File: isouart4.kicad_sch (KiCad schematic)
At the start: 14 parts, among them J1 USB_B, J2 Conn_01x04, J3 Conn_01x04, J4 Conn_01x04, J5 Conn_01x04, U3 AMS1117-3.3, U6 π122U31, U7 π122U31, U8 π122U31, U9 π122U31

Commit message: Flush
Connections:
- net indicators-ch2/GNDMON: now reaches J3.1 (Pin_1), U7.5 (GND2)
- net indicators-ch2/TXMON: now reaches J3.2 (Pin_2), U7.6 (VOB)
- net indicators-ch2/RXMON: now reaches J3.3 (Pin_3), U7.7 (VOA)
- net indicators-ch2/V+MON: now reaches J3.4 (Pin_4), U7.8 (VDD2)
- net indicators-ch1/TXMON: now reaches J2.2 (Pin_2), U6.6 (VOB)
- net indicators-ch1/RXMON: now reaches J2.3 (Pin_3), U6.7 (VIA)
- net indicators-ch1/V+MON: now reaches J2.4 (Pin_4), U6.8 (VDD2)
- net indicators-ch4/GNDMON: now reaches J5.1 (Pin_1), U9.5 (GND2)
- net indicators-ch4/TXMON: now reaches J5.2 (Pin_2), U9.6 (VOB)
- net indicators-ch4/RXMON: now reaches J5.3 (Pin_3), U9.7 (VOA)
- net indicators-ch4/V+MON: now reaches J5.4 (Pin_4), U9.8 (VDD2)
- net indicators-ch3/GNDMON: now reaches J4.1 (Pin_1), U8.5 (GND2)
- net indicators-ch3/TXMON: now reaches J4.2 (Pin_2), U8.6 (VOB)
- net indicators-ch3/RXMON: now reaches J4.3 (Pin_3), U8.7 (VOA)
- net indicators-ch3/V+MON: now reaches J4.4 (Pin_4), U8.8 (VDD2)
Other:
- sheet indicators-ch1 ports: added GNDMON, RXMON, TXMON, V+MON; removed none
- sheet indicators-ch2 ports: added GNDMON, RXMON, TXMON, V+MON; removed none
- sheet indicators-ch3 ports: added GNDMON, RXMON, TXMON, V+MON; removed none
- sheet indicators-ch4 ports: added GNDMON, RXMON, TXMON, V+MON; removed none

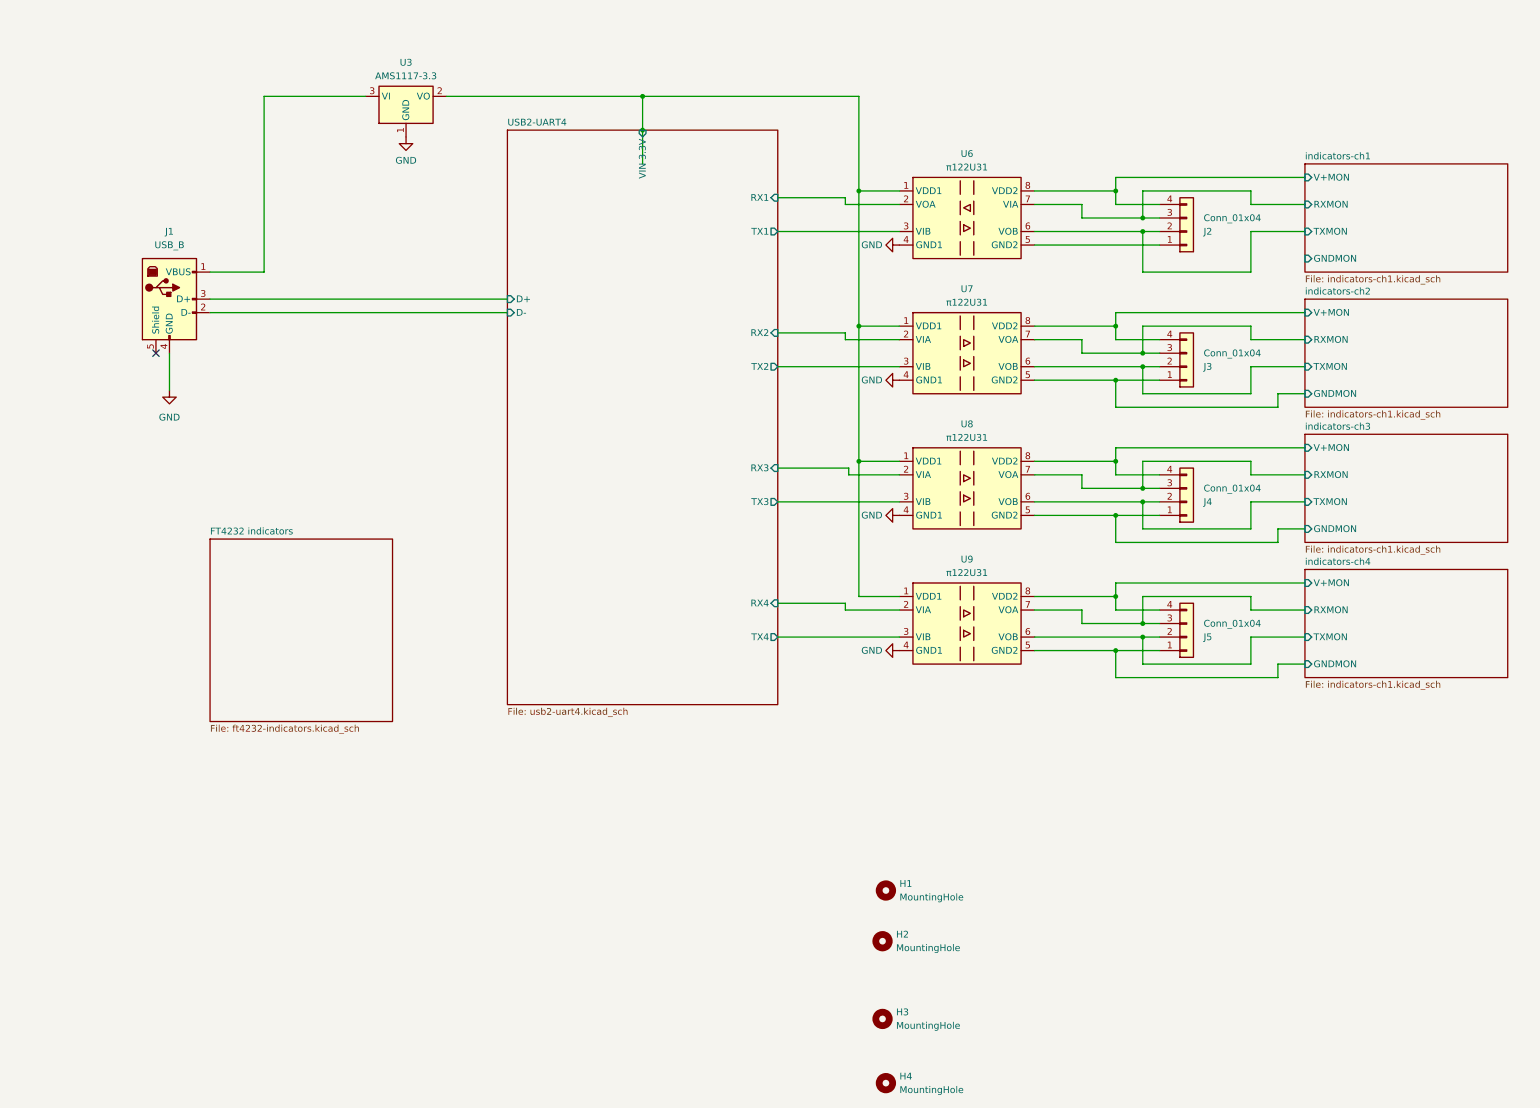
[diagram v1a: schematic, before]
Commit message: switch to CH344Q
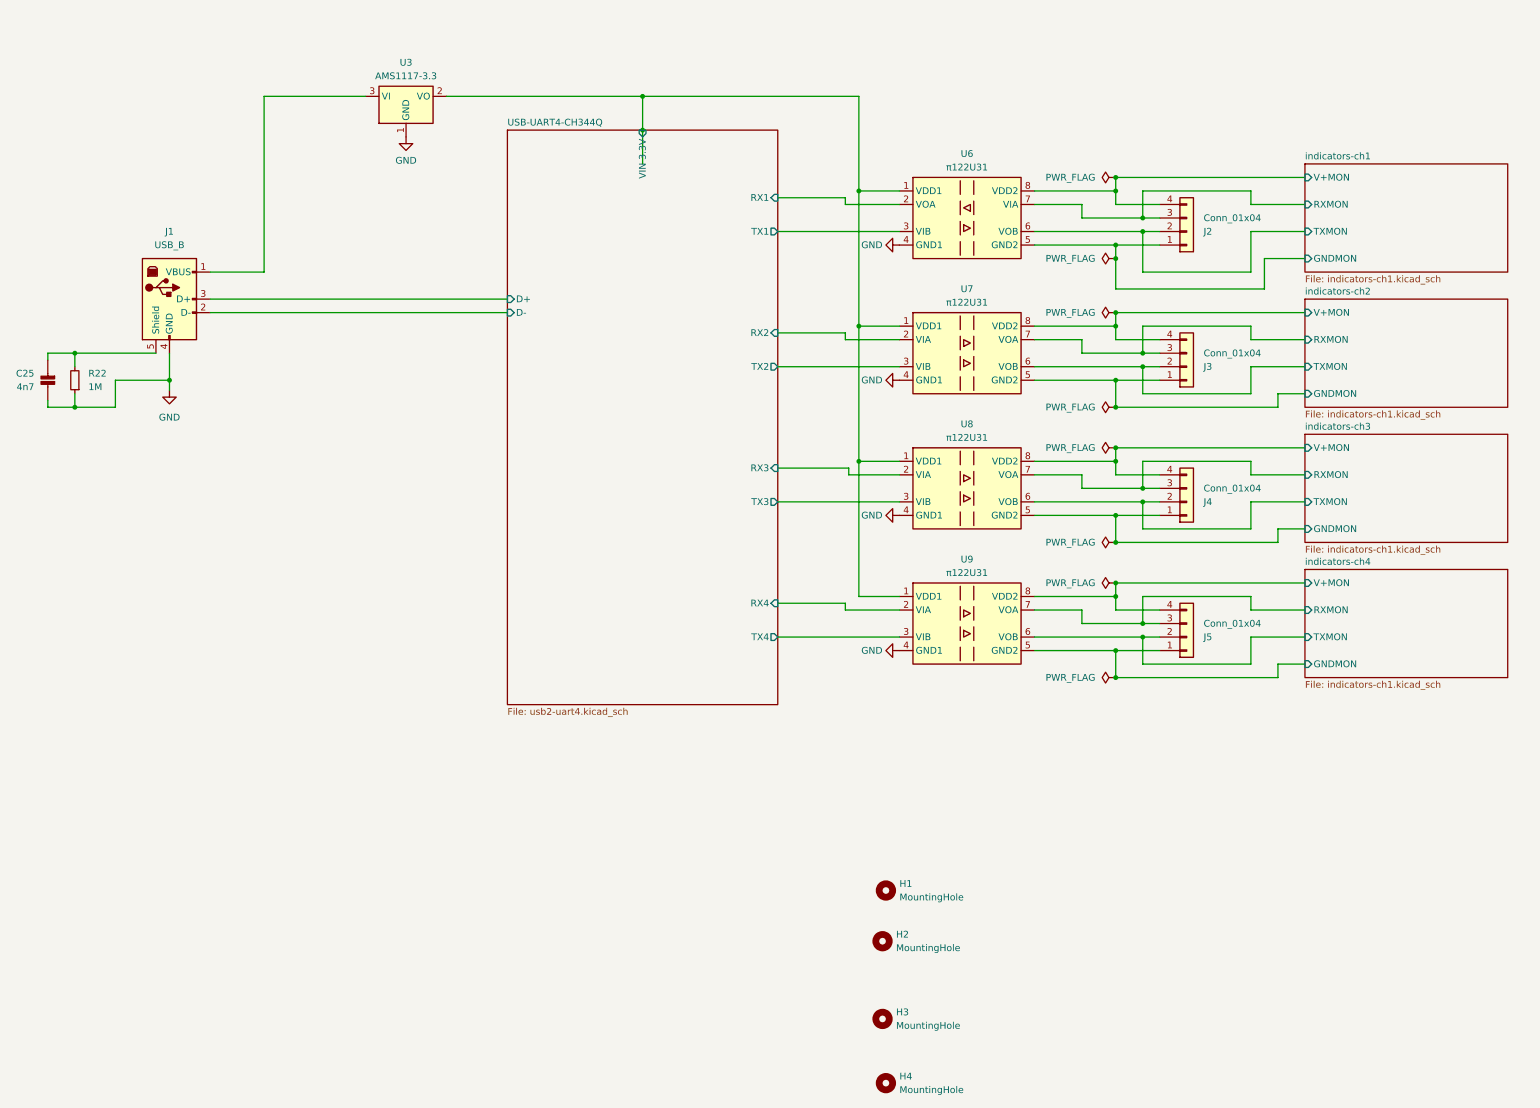
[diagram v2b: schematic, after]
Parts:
- added C25: 4n7, Capacitor_SMD:C_0805_2012Metric_Pad1.18x1.45mm_HandSolder, symbol H_passives:CAP_NP
- added R22: 1M, Resistor_SMD:R_0805_2012Metric_Pad1.20x1.40mm_HandSolder, symbol Device:R_Small
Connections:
- net GND: now also C25.1, R22.1
- net indicators-ch1/GNDMON: now also J2.1 (Pin_1), U6.5 (GND2)
- net at J1.5 (Shield): now also C25.2, R22.2
- no-connect marks 1 -> 0
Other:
- sheet USB2-UART4 renamed USB-UART4-CH344Q
- removed sheet FT4232 indicators

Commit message: More feng shui
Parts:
- removed C25: 4n7, Capacitor_SMD:C_0805_2012Metric_Pad1.18x1.45mm_HandSolder, symbol H_passives:CAP_NP
- removed R22: 1M, Resistor_SMD:R_0805_2012Metric_Pad1.20x1.40mm_HandSolder, symbol Device:R_Small
- removed U7, U8, U9: π122U31, Package_SO:SOIC-8_3.9x4.9mm_P1.27mm, symbol Isolator:π120U31
- added C2, C7: 10uF, Capacitor_SMD:C_0805_2012Metric_Pad1.18x1.45mm_HandSolder, symbol Device:C_Polarized_Small
- added C44: 100n, Capacitor_SMD:C_0603_1608Metric_Pad1.08x0.95mm_HandSolder, symbol H_passives:CAP_NP
- added L1, L2: L_Ferrite_Small, Inductor_SMD:L_TDK_NLV25_2.5x2.0mm, symbol Device:L_Ferrite_Small
- added U2, U4, U5: π122U31, Package_SO:SOIC-8_3.9x4.9mm_P1.27mm, symbol Isolator:π120U31
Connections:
- net GND: now also C2.2, C44.1, C7.2, L2.2, U2.4 (GND1), U4.4 (GND1), U5.4 (GND1); no longer J1.4 (GND)
- net USB-UART4-CH344Q/RX2: now also U2.2 (VIA)
- net USB-UART4-CH344Q/RX3: now also U4.2 (VIA)
- net USB-UART4-CH344Q/RX4: now also U5.2 (VIA)
- net USB-UART4-CH344Q/TX2: now also U2.3 (VIB)
- net USB-UART4-CH344Q/TX3: now also U4.3 (VIB)
- net USB-UART4-CH344Q/TX4: now also U5.3 (VIB)
- net USB-UART4-CH344Q/VIN 3.3V: now also C44.2, C7.1, U2.1 (VDD1), U4.1 (VDD1), U5.1 (VDD1)
- net indicators-ch2/GNDMON: now also U2.5 (GND2)
- net indicators-ch2/RXMON: now also U2.7 (VOA)
- net indicators-ch2/TXMON: now also U2.6 (VOB)
- net indicators-ch2/V+MON: now also U2.8 (VDD2)
- net indicators-ch3/GNDMON: now also U4.5 (GND2)
- net indicators-ch3/RXMON: now also U4.7 (VOA)
- net indicators-ch3/TXMON: now also U4.6 (VOB)
- net indicators-ch3/V+MON: now also U4.8 (VDD2)
- net indicators-ch4/GNDMON: now also U5.5 (GND2)
- net indicators-ch4/RXMON: now also U5.7 (VOA)
- net indicators-ch4/TXMON: now also U5.6 (VOB)
- net indicators-ch4/V+MON: now also U5.8 (VDD2)
- net at J1.1 (VBUS): now also L1.1; no longer U3.3 (VI)
- net USBSHLD: now reaches J1.5 (Shield)
- new net: C2.1, L1.2, U3.3 (VI)
- new net GNDUSBCONN: J1.4 (GND), L2.1
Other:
- sheet USB-UART4-CH344Q ports: added GNDUSBUART, SHLDUSB; removed none
- moved on the sheet: H1, H2, H3, H4

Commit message: pcb-route all uart channels
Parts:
- added C44 (x3): 100n, Capacitor_SMD:C_0805_2012Metric_Pad1.18x1.45mm_HandSolder, symbol H_passives:CAP_NP
- C44: footprint Capacitor_SMD:C_0603_1608Metric_Pad1.08x0.95mm_HandSolder -> Capacitor_SMD:C_0805_2012Metric_Pad1.18x1.45mm_HandSolder
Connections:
- net GND: now also C44.1, C44.1, C44.1
- net USB-UART4-CH344Q/VIN 3.3V: now also C44.2, C44.2, C44.2

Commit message: Flush latest changes
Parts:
- added C25: 4n7, Capacitor_SMD:C_0805_2012Metric_Pad1.18x1.45mm_HandSolder, symbol H_passives:CAP_NP
- added F1: 500mA, anotherfuse:FuseX, symbol Device:Fuse_Small
- added R22: 4K7, Resistor_SMD:R_0805_2012Metric_Pad1.20x1.40mm_HandSolder, symbol Device:R_Small
- H1, H2, H3, H4: footprint MountingHole:MountingHole_3.2mm_M3 -> MountingHole:MountingHole_3.2mm_M3_Pad_Via; symbol Mechanical:MountingHole -> Mechanical:MountingHole_Pad; now left out of the parts list
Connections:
- net USBSHLD: now also C25.2, R22.2
- net at J1.1 (VBUS): now also F1.1; no longer L1.1
- new net: F1.2, L1.1
- new net SHLD: C25.1, H1.1, H2.1, H3.1, H4.1, R22.1

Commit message: Add π122U31 to the project lib
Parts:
- U2, U4, U5, U6: symbol Isolator:π120U31 -> isouart4:π122U31
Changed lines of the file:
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@@
     )
   )
-  (symbol (lib_id "Isolator:π120U31") (at 213.36 137.16 0) (unit 1)
-    (in_bom yes) (on_board yes) (dnp no) (fields_autoplaced)
-    (property "Reference" "U2" (at 213.36 125.095 0)
-      (effects (font (size 1.27 1.27)))
-    )
-    (property "Value" "π122U31" (at 213.36 127.635 0)
+  (symbol (lib_id "isouart4:π122U31") (at 213.36 137.16 0) (unit 1)
+    (in_bom yes) (on_board yes) (dnp no) (fields_autoplaced)
+    (property "Reference" "U2" (at 213.36 124.46 0)
+      (effects (font (size 1.27 1.27)))
+    )
+    (property "Value" "π122U31" (at 213.36 127 0)
       (effects (font (size 1.27 1.27)))
     )
@@
     )
   )
-  (symbol (lib_id "Isolator:π120U31") (at 213.36 111.76 0) (unit 1)
-    (in_bom yes) (on_board yes) (dnp no) (fields_autoplaced)
-    (property "Reference" "U6" (at 213.36 99.695 0)
-      (effects (font (size 1.27 1.27)))
-    )
-    (property "Value" "π122U31" (at 213.36 102.235 0)
+  (symbol (lib_id "isouart4:π122U31") (at 213.36 111.76 0) (unit 1)
+    (in_bom yes) (on_board yes) (dnp no) (fields_autoplaced)
+    (property "Reference" "U6" (at 213.36 99.06 0)
+      (effects (font (size 1.27 1.27)))
+    )
+    (property "Value" "π122U31" (at 213.36 101.6 0)
       (effects (font (size 1.27 1.27)))
     )
@@
     )
   )
-  (symbol (lib_id "Isolator:π120U31") (at 213.36 187.96 0) (unit 1)
-    (in_bom yes) (on_board yes) (dnp no) (fields_autoplaced)
-    (property "Reference" "U5" (at 213.36 175.895 0)
-      (effects (font (size 1.27 1.27)))
-    )
-    (property "Value" "π122U31" (at 213.36 178.435 0)
+  (symbol (lib_id "isouart4:π122U31") (at 213.36 187.96 0) (unit 1)
+    (in_bom yes) (on_board yes) (dnp no) (fields_autoplaced)
+    (property "Reference" "U5" (at 213.36 175.26 0)
+      (effects (font (size 1.27 1.27)))
+    )
+    (property "Value" "π122U31" (at 213.36 177.8 0)
       (effects (font (size 1.27 1.27)))
     )
@@
     )
   )
-  (symbol (lib_id "Isolator:π120U31") (at 213.36 162.56 0) (unit 1)
-    (in_bom yes) (on_board yes) (dnp no) (fields_autoplaced)
-    (property "Reference" "U4" (at 213.36 150.495 0)
-      (effects (font (size 1.27 1.27)))
-    )
-    (property "Value" "π122U31" (at 213.36 153.035 0)
-      (effects (font (size 1.27 1.27)))
-    )
+  (symbol (lib_id "isouart4:π122U31") (at 213.36 162.56 0) (unit 1)
+    (in_bom yes) (on_board yes) (dnp no) (fields_autoplaced)
+    (property "Reference" "U4" (at 213.36 149.86 0)
+      (effects (font (size 1.27 1.27)))
+    )
+    (property "Value" "π122U31" (at 213.36 152.4 0)
+      (effects (font (size 1.27 1.27)))
+    )

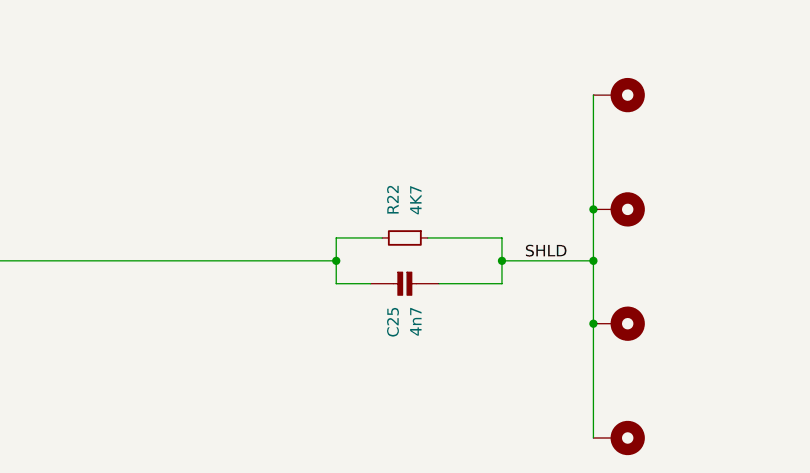
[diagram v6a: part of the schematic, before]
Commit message: H_passives:CAP_NP -> isouart4:CAP_NP
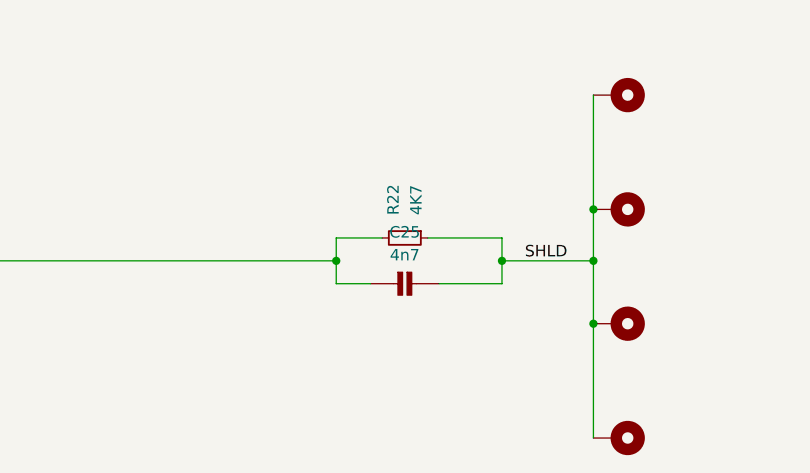
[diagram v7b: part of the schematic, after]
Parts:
- C25, C44: footprint Capacitor_SMD:C_0805_2012Metric_Pad1.18x1.45mm_HandSolder -> Capacitor_SMD:C_0603_1608Metric_Pad1.08x0.95mm_HandSolder; symbol H_passives:CAP_NP -> isouart4:CAP_NP
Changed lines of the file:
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@@
     )
   )
-  (symbol (lib_id "H_passives:CAP_NP") (at 167.005 255.905 270) (unit 1)
-    (in_bom yes) (on_board yes) (dnp no) (fields_autoplaced)
-    (property "Reference" "C25" (at 165.7349 258.445 0)
-      (effects (font (size 1.27 1.27)) (justify left))
-    )
-    (property "Value" "4n7" (at 168.2749 258.445 0)
-      (effects (font (size 1.27 1.27)) (justify left))
-    )
-    (property "Footprint" "Capacitor_SMD:C_0805_2012Metric_Pad1.18x1.45mm_HandSolder" (at 165.735 255.905 0)
+  (symbol (lib_id "isouart4:CAP_NP") (at 167.005 255.905 270) (unit 1)
+    (in_bom yes) (on_board yes) (dnp no) (fields_autoplaced)
+    (property "Reference" "C25" (at 167.005 250.19 90)
+      (effects (font (size 1.27 1.27)))
+    )
+    (property "Value" "4n7" (at 167.005 252.73 90)
+      (effects (font (size 1.27 1.27)))
+    )
+    (property "Footprint" "Capacitor_SMD:C_0603_1608Metric_Pad1.08x0.95mm_HandSolder" (at 165.735 255.905 0)
       (effects (font (size 1.27 1.27)) hide)
     )
@@
     )
   )
-  (symbol (lib_id "H_passives:CAP_NP") (at 199.39 176.53 0) (unit 1)
+  (symbol (lib_id "isouart4:CAP_NP") (at 199.39 176.53 0) (unit 1)
     (in_bom yes) (on_board yes) (dnp no)
     (property "Reference" "C44" (at 198.12 179.07 90)
@@
       (effects (font (size 1.27 1.27)))
     )
-    (property "Footprint" "Capacitor_SMD:C_0805_2012Metric_Pad1.18x1.45mm_HandSolder" (at 199.39 177.8 0)
+    (property "Footprint" "Capacitor_SMD:C_0603_1608Metric_Pad1.08x0.95mm_HandSolder" (at 199.39 177.8 0)
       (effects (font (size 1.27 1.27)) hide)
     )
@@
     )
   )
-  (symbol (lib_id "H_passives:CAP_NP") (at 199.39 125.73 0) (unit 1)
+  (symbol (lib_id "isouart4:CAP_NP") (at 199.39 125.73 0) (unit 1)
     (in_bom yes) (on_board yes) (dnp no)
     (property "Reference" "C44" (at 198.12 128.27 90)
@@
       (effects (font (size 1.27 1.27)))
     )
-    (property "Footprint" "Capacitor_SMD:C_0805_2012Metric_Pad1.18x1.45mm_HandSolder" (at 199.39 127 0)
+    (property "Footprint" "Capacitor_SMD:C_0603_1608Metric_Pad1.08x0.95mm_HandSolder" (at 199.39 127 0)
       (effects (font (size 1.27 1.27)) hide)
     )
@@
     )
   )
-  (symbol (lib_id "H_passives:CAP_NP") (at 199.39 151.13 0) (unit 1)
+  (symbol (lib_id "isouart4:CAP_NP") (at 199.39 151.13 0) (unit 1)
     (in_bom yes) (on_board yes) (dnp no)
     (property "Reference" "C44" (at 198.12 153.67 90)
@@
       (effects (font (size 1.27 1.27)))
     )
-    (property "Footprint" "Capacitor_SMD:C_0805_2012Metric_Pad1.18x1.45mm_HandSolder" (at 199.39 152.4 0)
+    (property "Footprint" "Capacitor_SMD:C_0603_1608Metric_Pad1.08x0.95mm_HandSolder" (at 199.39 152.4 0)
       (effects (font (size 1.27 1.27)) hide)
     )
@@
     )
   )
-  (symbol (lib_id "H_passives:CAP_NP") (at 199.39 100.33 0) (unit 1)
+  (symbol (lib_id "isouart4:CAP_NP") (at 199.39 100.33 0) (unit 1)
     (in_bom yes) (on_board yes) (dnp no)
     (property "Reference" "C44" (at 198.12 102.87 90)
@@
       (effects (font (size 1.27 1.27)))
     )
-    (property "Footprint" "Capacitor_SMD:C_0805_2012Metric_Pad1.18x1.45mm_HandSolder" (at 199.39 101.6 0)
-      (effects (font (size 1.27 1.27)) hide)
-    )
+    (property "Footprint" "Capacitor_SMD:C_0603_1608Metric_Pad1.08x0.95mm_HandSolder" (at 199.39 101.6 0)
+      (effects (font (size 1.27 1.27)) hide)
+    )
